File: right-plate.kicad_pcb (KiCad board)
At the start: 2 copper layers, 208.8 x 114.3 mm, 42 parts

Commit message: rename files
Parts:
- REF** (x42): footprint myles-keyboard:KeyHole -> keyboard:KeyHole

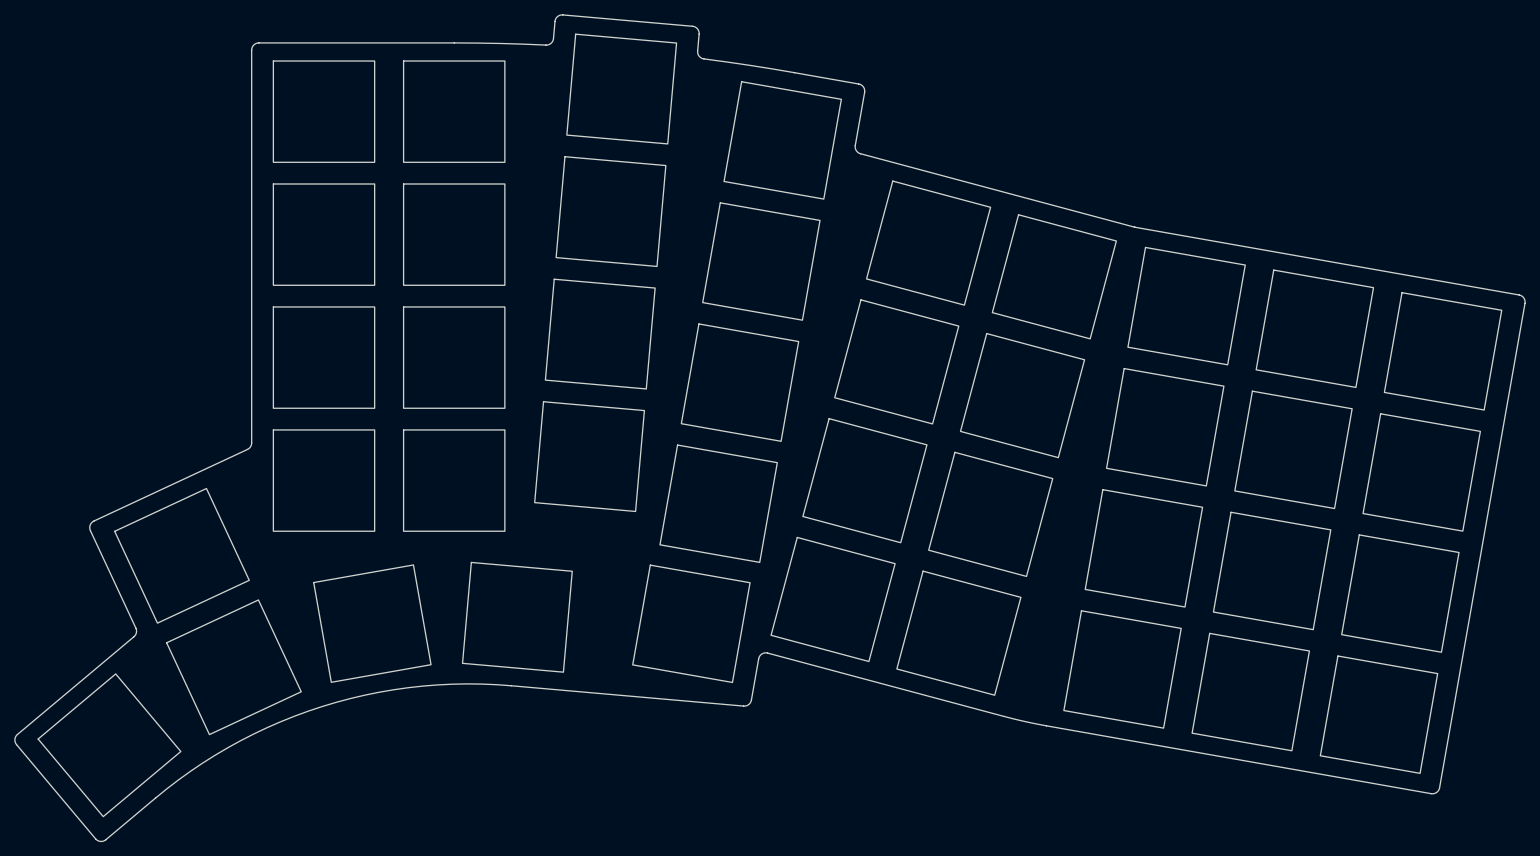
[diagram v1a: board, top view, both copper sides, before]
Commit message: adjust plates and pcb; remove reset button
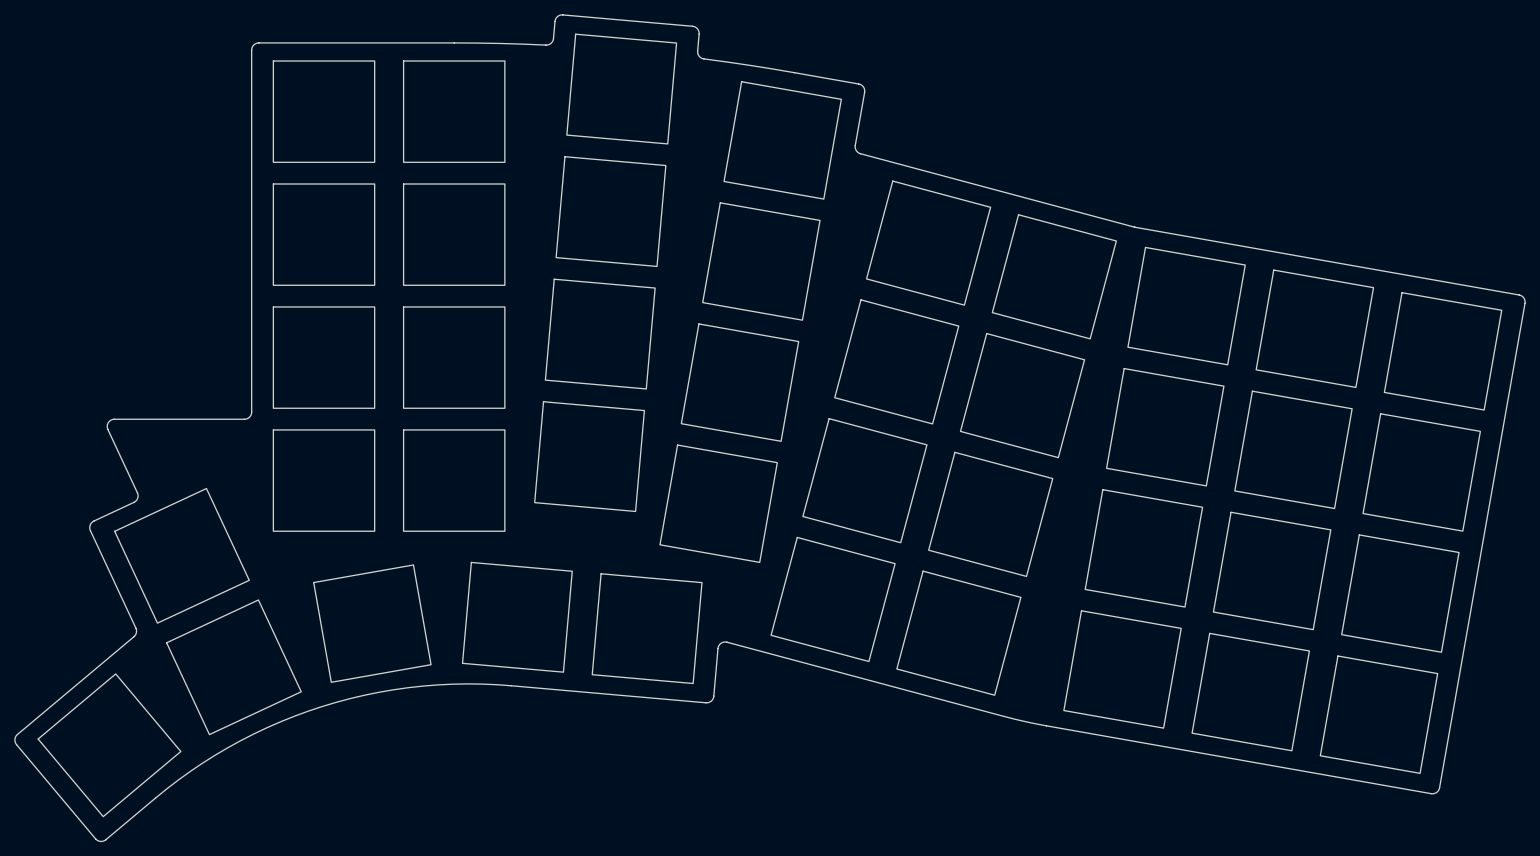
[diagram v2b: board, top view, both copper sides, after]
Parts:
- moved REF** 6.16 mm to (124.4, 114.0), turned to -5 degrees
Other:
- outline, holes or cut-outs redrawn

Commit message: update plates
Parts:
- moved REF** 1.76 mm to (51.5, 128.9)
- moved REF** 1.56 mm to (107.6, 111.3)
- moved REF** 1.56 mm to (68.4, 118.2)
- moved REF** 1.56 mm to (61.2, 102.8)
- moved REF** 1.56 mm to (87.5, 112.1)
- moved REF** 1.54 mm to (125.7, 113.0), turned to -6.171 degrees
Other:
- board size 208.8 x 114.3 mm -> 207.7 x 113.1 mm
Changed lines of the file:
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@@
   )
   (footprint "keyboard:KeyHole" (layer "F.Cu")
-    (at 60.145785 103.89932 25)
+    (at 61.201051 102.753693 25)
     (fp_text reference "REF**" (at 0 0 25 unlocked) (layer "F.Fab") hide
       (effects (font (size 1 1) (thickness 0.1)))
@@
   )
   (footprint "keyboard:KeyHole" (layer "F.Cu")
-    (at 106.512436 112.397684 -5)
+    (at 107.567703 111.252057 -5)
     (fp_text reference "REF**" (at 0 0 -5 unlocked) (layer "F.Fab") hide
       (effects (font (size 1 1) (thickness 0.1)))
@@
   )
   (footprint "keyboard:KeyHole" (layer "F.Cu")
-    (at 124.443941 113.966487 -5)
-    (fp_text reference "REF**" (at 0 0 -5 unlocked) (layer "F.Fab") hide
-      (effects (font (size 1 1) (thickness 0.1)))
-    )
-    (fp_text value "KeyHole" (at 0 2 -5 unlocked) (layer "F.Fab") hide
+    (at 125.654248 113.020897 -6.171)
+    (fp_text reference "REF**" (at 0 0 -6.171 unlocked) (layer "F.Fab") hide
+      (effects (font (size 1 1) (thickness 0.1)))
+    )
+    (fp_text value "KeyHole" (at 0 2 -6.171 unlocked) (layer "F.Fab") hide
       (effects (font (size 1 1) (thickness 0.125)))
     )
@@
   )
   (footprint "keyboard:KeyHole" (layer "F.Cu")
-    (at 67.330295 119.306552 25)
+    (at 68.385562 118.160925 25)
     (fp_text reference "REF**" (at 0 0 25 unlocked) (layer "F.Fab") hide
       (effects (font (size 1 1) (thickness 0.1)))
@@
   )
   (footprint "keyboard:KeyHole" (layer "F.Cu")
-    (at 86.466581 113.272904 10)
+    (at 87.521848 112.127278 10)
     (fp_text reference "REF**" (at 0 0 10 unlocked) (layer "F.Fab") hide
       (effects (font (size 1 1) (thickness 0.1)))
@@
   )
   (footprint "keyboard:KeyHole" (layer "F.Cu")
-    (at 50.124844 130.087443 40)
+    (at 51.462952 128.941816 40)
     (fp_text reference "REF**" (at 0 0 40 unlocked) (layer "F.Fab") hide
       (effects (font (size 1 1) (thickness 0.1)))
@@
     (fp_rect (start -7 -7) (end 7 7) (layer "Edge.Cuts") (stroke (width 0.12) (type default)) (fill none))
   )
-  (gr_line (start 49.909173 86.442618) (end 53.986308 95.186063) (layer "Edge.Cuts") (width 0.12))
-  (gr_line (start 47.490452 100.421886) (end 53.772947 113.894741) (layer "Edge.Cuts") (width 0.12))
+  (gr_line (start 51.498654 86.442618) (end 55.041575 94.040436) (layer "Edge.Cuts") (width 0.12))
+  (gr_line (start 48.545718 99.276259) (end 54.828214 112.749115) (layer "Edge.Cuts") (width 0.12))
   (gr_line (start 144.838586 37.117093) (end 153.701856 38.679926) (layer "Edge.Cuts") (width 0.12))
   (gr_line (start 179.650884 127.400816) (end 232.830502 136.777818) (layer "Edge.Cuts") (width 0.12))
   (gr_arc (start 244.985875 67.841276) (mid 245.631378 68.252507) (end 245.797034 68.999731) (layer "Edge.Cuts") (width 0.12))
   (gr_arc (start 111.710396 30.037309) (mid 112.063803 29.35842) (end 112.793746 29.12827) (layer "Edge.Cuts") (width 0.12))
-  (gr_arc (start 134.24122 116.720205) (mid 134.663841 115.988213) (end 135.496234 115.841441) (layer "Edge.Cuts") (width 0.12))
   (gr_arc (start 191.892252 58.479437) (mid 191.849455 58.470924) (end 191.80707 58.460552) (layer "Edge.Cuts") (width 0.12))
   (gr_line (start 70.78 33) (end 97.78 33) (layer "Edge.Cuts") (width 0.12))
@@
   (gr_arc (start 153.945198 48.315494) (mid 153.360626 47.886868) (end 153.219209 47.17592) (layer "Edge.Cuts") (width 0.12))
   (gr_arc (start 153.701856 38.679926) (mid 154.34736 39.091158) (end 154.513015 39.838382) (layer "Edge.Cuts") (width 0.12))
-  (gr_arc (start 53.772946 113.894741) (mid 53.842935 114.533799) (end 53.509427 115.083404) (layer "Edge.Cuts") (width 0.12))
-  (gr_line (start 53.509427 115.083404) (end 37.406804 128.59511) (layer "Edge.Cuts") (width 0.12))
+  (gr_line (start 54.564694 113.937777) (end 38.462071 127.449483) (layer "Edge.Cuts") (width 0.12))
+  (gr_arc (start 57.569435 136.219239) (mid 80.612677 123.577284) (end 106.739723 120.715907) (layer "Edge.Cuts") (width 0.12))
   (gr_line (start 131.42888 34.128269) (end 131.63429 31.780424) (layer "Edge.Cuts") (width 0.12))
-  (gr_line (start 68.78 85.02) (end 50.815481 85.02) (layer "Edge.Cuts") (width 0.12))
+  (gr_line (start 68.78 85.02) (end 52.404962 85.02) (layer "Edge.Cuts") (width 0.12))
   (gr_line (start 191.80707 58.460552) (end 153.945198 48.315494) (layer "Edge.Cuts") (width 0.12))
-  (gr_line (start 134.24122 116.720205) (end 133.665064 123.305699) (layer "Edge.Cuts") (width 0.12))
+  (gr_arc (start 50.675034 142.004326) (mid 49.945092 142.234476) (end 49.266203 141.88107) (layer "Edge.Cuts") (width 0.12))
+  (gr_arc (start 54.828214 112.749115) (mid 54.898202 113.388172) (end 54.564694 113.937777) (layer "Edge.Cuts") (width 0.12))
+  (gr_arc (start 48.545718 99.276259) (mid 48.512334 98.511621) (end 49.029408 97.947333) (layer "Edge.Cuts") (width 0.12))
+  (gr_line (start 135.17438 116.970262) (end 134.720331 122.160072) (layer "Edge.Cuts") (width 0.12))
   (gr_arc (start 233.988959 135.966658) (mid 233.577727 136.612162) (end 232.830502 136.777818) (layer "Edge.Cuts") (width 0.12))
   (gr_arc (start 97.78 33) (mid 104.122734 33.074236) (end 110.461994 33.296903) (layer "Edge.Cuts") (width 0.12))
-  (gr_line (start 53.502619 96.514989) (end 47.974141 99.09296) (layer "Edge.Cuts") (width 0.12))
-  (gr_line (start 173.774094 126.097962) (end 135.496234 115.841441) (layer "Edge.Cuts") (width 0.12))
+  (gr_line (start 54.557885 95.369362) (end 49.029408 97.947333) (layer "Edge.Cuts") (width 0.12))
+  (gr_line (start 173.774094 126.097962) (end 136.429395 116.091481) (layer "Edge.Cuts") (width 0.12))
+  (gr_arc (start 134.720331 122.160072) (mid 134.366924 122.838961) (end 133.63698 123.069112) (layer "Edge.Cuts") (width 0.12))
   (gr_arc (start 130.725251 30.697074) (mid 131.40414 31.050481) (end 131.63429 31.780424) (layer "Edge.Cuts") (width 0.12))
-  (gr_line (start 132.581714 124.214738) (end 105.684457 121.861533) (layer "Edge.Cuts") (width 0.12))
+  (gr_line (start 133.63698 123.069111) (end 106.739723 120.715906) (layer "Edge.Cuts") (width 0.12))
   (gr_line (start 111.710396 30.037309) (end 111.504986 32.385154) (layer "Edge.Cuts") (width 0.12))
+  (gr_arc (start 38.338814 128.858315) (mid 38.108663 128.128371) (end 38.462071 127.449482) (layer "Edge.Cuts") (width 0.12))
   (gr_arc (start 111.504986 32.385154) (mid 111.16694 33.050886) (end 110.461994 33.296902) (layer "Edge.Cuts") (width 0.12))
-  (gr_arc (start 47.490452 100.421886) (mid 47.457067 99.657248) (end 47.974141 99.09296) (layer "Edge.Cuts") (width 0.12))
   (gr_line (start 69.78 84.02) (end 69.78 34) (layer "Edge.Cuts") (width 0.12))
-  (gr_line (start 49.619768 143.149954) (end 56.514168 137.364866) (layer "Edge.Cuts") (width 0.12))
+  (gr_line (start 50.675034 142.004326) (end 57.569435 136.219239) (layer "Edge.Cuts") (width 0.12))
+  (gr_arc (start 51.498654 86.442618) (mid 51.56157 85.4827) (end 52.404962 85.02) (layer "Edge.Cuts") (width 0.12))
   (gr_line (start 191.892252 58.479437) (end 244.985875 67.841276) (layer "Edge.Cuts") (width 0.12))
   (gr_arc (start 69.78 84.02) (mid 69.487107 84.727107) (end 68.78 85.02) (layer "Edge.Cuts") (width 0.12))
   (gr_arc (start 69.78 34) (mid 70.072893 33.292893) (end 70.78 33) (layer "Edge.Cuts") (width 0.12))
   (gr_arc (start 132.2977 35.20728) (mid 138.579319 36.088797) (end 144.838586 37.117094) (layer "Edge.Cuts") (width 0.12))
-  (gr_line (start 48.210936 143.026697) (end 37.283547 130.003942) (layer "Edge.Cuts") (width 0.12))
+  (gr_line (start 49.266202 141.88107) (end 38.338813 128.858315) (layer "Edge.Cuts") (width 0.12))
   (gr_arc (start 179.650884 127.400815) (mid 176.698275 126.813504) (end 173.774094 126.097962) (layer "Edge.Cuts") (width 0.12))
-  (gr_arc (start 133.665064 123.305699) (mid 133.311657 123.984588) (end 132.581714 124.214738) (layer "Edge.Cuts") (width 0.12))
   (gr_line (start 154.513015 39.838382) (end 153.219209 47.17592) (layer "Edge.Cuts") (width 0.12))
-  (gr_arc (start 53.986308 95.186063) (mid 54.019693 95.950701) (end 53.502619 96.514988) (layer "Edge.Cuts") (width 0.12))
-  (gr_arc (start 49.909173 86.442618) (mid 49.97209 85.4827) (end 50.815481 85.02) (layer "Edge.Cuts") (width 0.12))
-  (gr_arc (start 49.619768 143.149954) (mid 48.889825 143.380104) (end 48.210937 143.026696) (layer "Edge.Cuts") (width 0.12))
+  (gr_arc (start 135.17438 116.970262) (mid 135.596995 116.238258) (end 136.429395 116.091481) (layer "Edge.Cuts") (width 0.12))
+  (gr_arc (start 55.041575 94.040436) (mid 55.074959 94.805074) (end 54.557885 95.369362) (layer "Edge.Cuts") (width 0.12))
   (gr_line (start 130.725251 30.697074) (end 112.793746 29.12827) (layer "Edge.Cuts") (width 0.12))
   (gr_line (start 233.988959 135.966658) (end 245.797034 68.999731) (layer "Edge.Cuts") (width 0.12))
-  (gr_arc (start 56.514168 137.364866) (mid 79.55741 124.72291) (end 105.684457 121.861534) (layer "Edge.Cuts") (width 0.12))
-  (gr_arc (start 37.283548 130.003941) (mid 37.053398 129.273999) (end 37.406804 128.59511) (layer "Edge.Cuts") (width 0.12))
 )
